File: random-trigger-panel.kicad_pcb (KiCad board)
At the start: 2 copper layers, 50.5 x 128.5 mm, 23 parts

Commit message: Add trigger normalling and switch to using kicad-libraries
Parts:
- ? (x5), REF**: value PanelHole_Jack -> PanelHole_PJ301BM_Output; footprint Extras:PanelHole_Jack -> MAI_PanelHole:PanelHole_PJ301BM_Output; moved to F.Cu
- REF** (x4): value PanelHole_Jack -> PanelHole_PJ301BM; footprint Extras:PanelHole_Jack -> MAI_PanelHole:PanelHole_PJ301BM; moved to F.Cu
- REF** (x2): value PanelHole_Pot -> PanelHole_Potentiometer_Alpha_RD901F-40-00D_Single_Vertical; footprint Extras:PanelHole_Pot -> MAI_PanelHole:PanelHole_Potentiometer_Alpha_RD901F-40-00D_Single_Vertical
- REF** (x6): value PanelHole_LED -> PanelHole_LED_D3.0mm; footprint Extras:PanelHole_LED -> MAI_PanelHole:PanelHole_LED_D3.0mm
- REF**: value logo_panel -> MAI_Logo_10.5mm_Soldermask; footprint Extras:logo_panel -> MAI_Logo:MAI_Logo_10.5mm_Soldermask
- moved REF** 3.07 mm to (125.2, 160.0)
- moved REF** 1.27 mm to (134.5, 144.5), turned to 90 degrees
- moved REF** 1.27 mm to (134.5, 128.8), turned to 90 degrees
- moved REF** 1.27 mm to (134.5, 97.4), turned to 90 degrees
- moved REF** 1.27 mm to (134.5, 66.0), turned to 90 degrees
- moved REF** 1.27 mm to (134.5, 113.1), turned to 90 degrees
- moved REF** 1.27 mm to (134.5, 81.7), turned to 90 degrees
- turned ? to 0 degrees (x5)
- turned REF** to 0 degrees (x2)
- turned REF** to 90 degrees
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
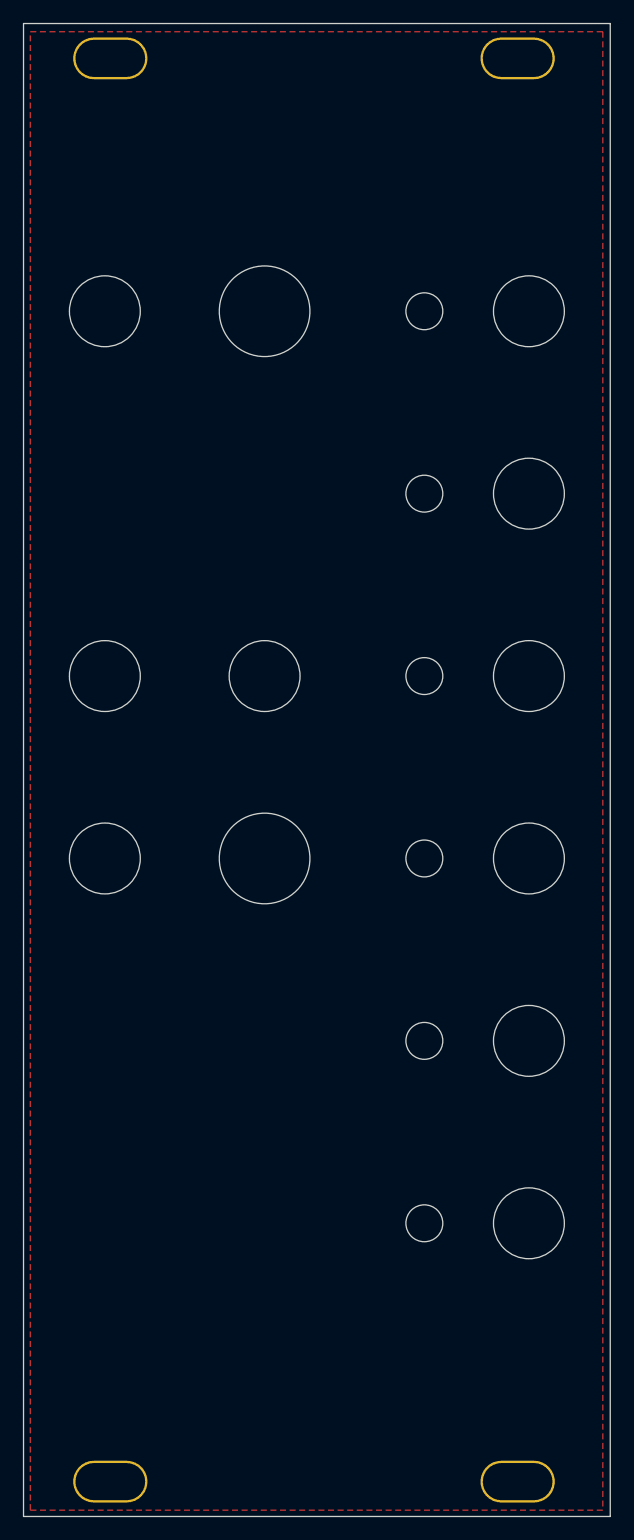
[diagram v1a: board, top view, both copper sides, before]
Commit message: Redo PCB to have all components on front
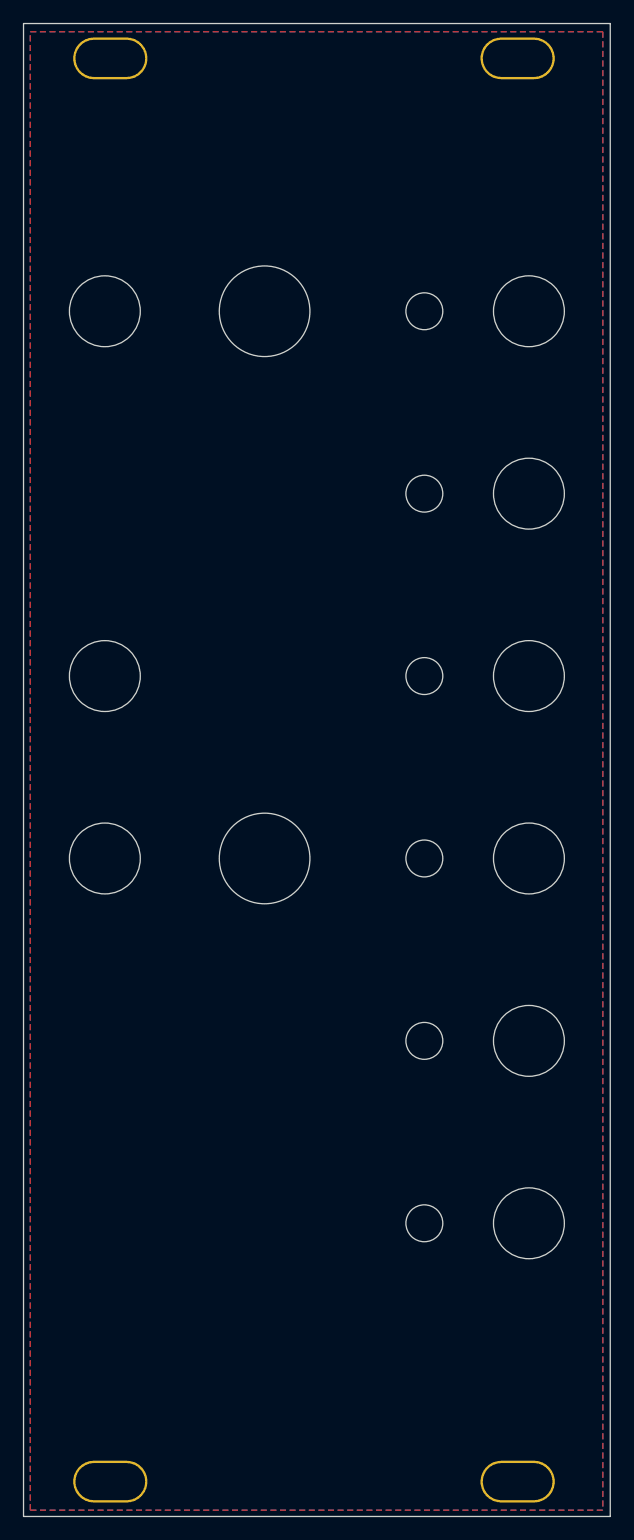
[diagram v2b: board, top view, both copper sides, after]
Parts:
- removed the REF** at (120.8, 96.1)
- REF** (x8): moved to F.Cu
- turned REF** to -90 degrees
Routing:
- added copper zone on B.Cu, net (none)
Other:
- board text removed: "Noise In"

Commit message: Add square to noise out
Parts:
- REF**: value PanelHole_PJ301BM -> PanelHole_PJ301BM_Output; footprint MAI_PanelHole:PanelHole_PJ301BM -> MAI_PanelHole:PanelHole_PJ301BM_Output
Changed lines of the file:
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@@
 		(embedded_fonts no)
 	)
-	(footprint "MAI_PanelHole:PanelHole_PJ301BM"
+	(footprint "MAI_PanelHole:PanelHole_PJ301BM_Output"
 		(locked yes)
 		(layer "F.Cu")
@@
 			)
 		)
-		(property "Value" "PanelHole_PJ301BM"
+		(property "Value" "PanelHole_PJ301BM_Output"
 			(at 0 1 0)
 			(unlocked yes)
@@
 		(attr board_only exclude_from_pos_files exclude_from_bom allow_missing_courtyard)
 		(fp_rect
+			(start -3.75 -3.75)
+			(end 3.75 3.75)
+			(stroke
+				(width 1)
+				(type solid)
+			)
+			(fill yes)
+			(layer "F.Mask")
+		)
+		(fp_rect
 			(start -5.4 -6.2)
